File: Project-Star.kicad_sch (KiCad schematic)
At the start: 148 parts, among them J1 J_TH1, J2 J_TH2, Q1 DMN2004K, Q10 CSD18540Q5B, Q11 ZXMP10A13F, Q12 BSS123, Q13 ZXMP10A13F, Q2 DMN2004K, Q3 DMN2004K, Q4 DMN2004K, Q5 CSD19531Q5A, Q6 DMN2004K, Q7 DMN2004K, Q8 DMN2004K, Q9 DMN2004K, SW1 SW_SPST, U1 BQ7693006DBTR, U2 BQ76200PW, U3 LM5164DDA

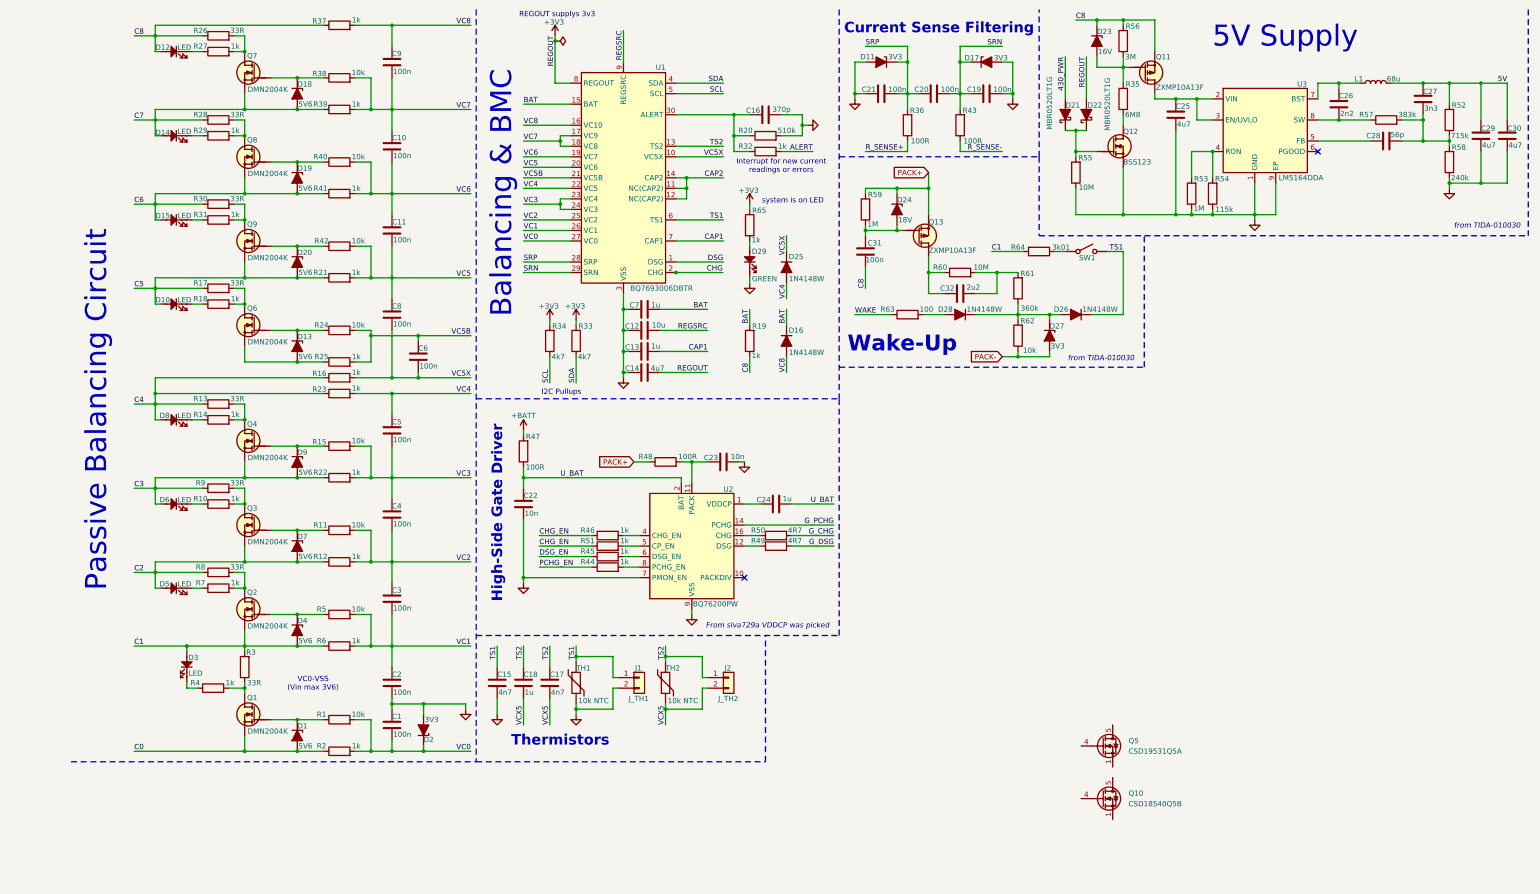
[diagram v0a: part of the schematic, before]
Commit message: cgr, dsg fets + jtag
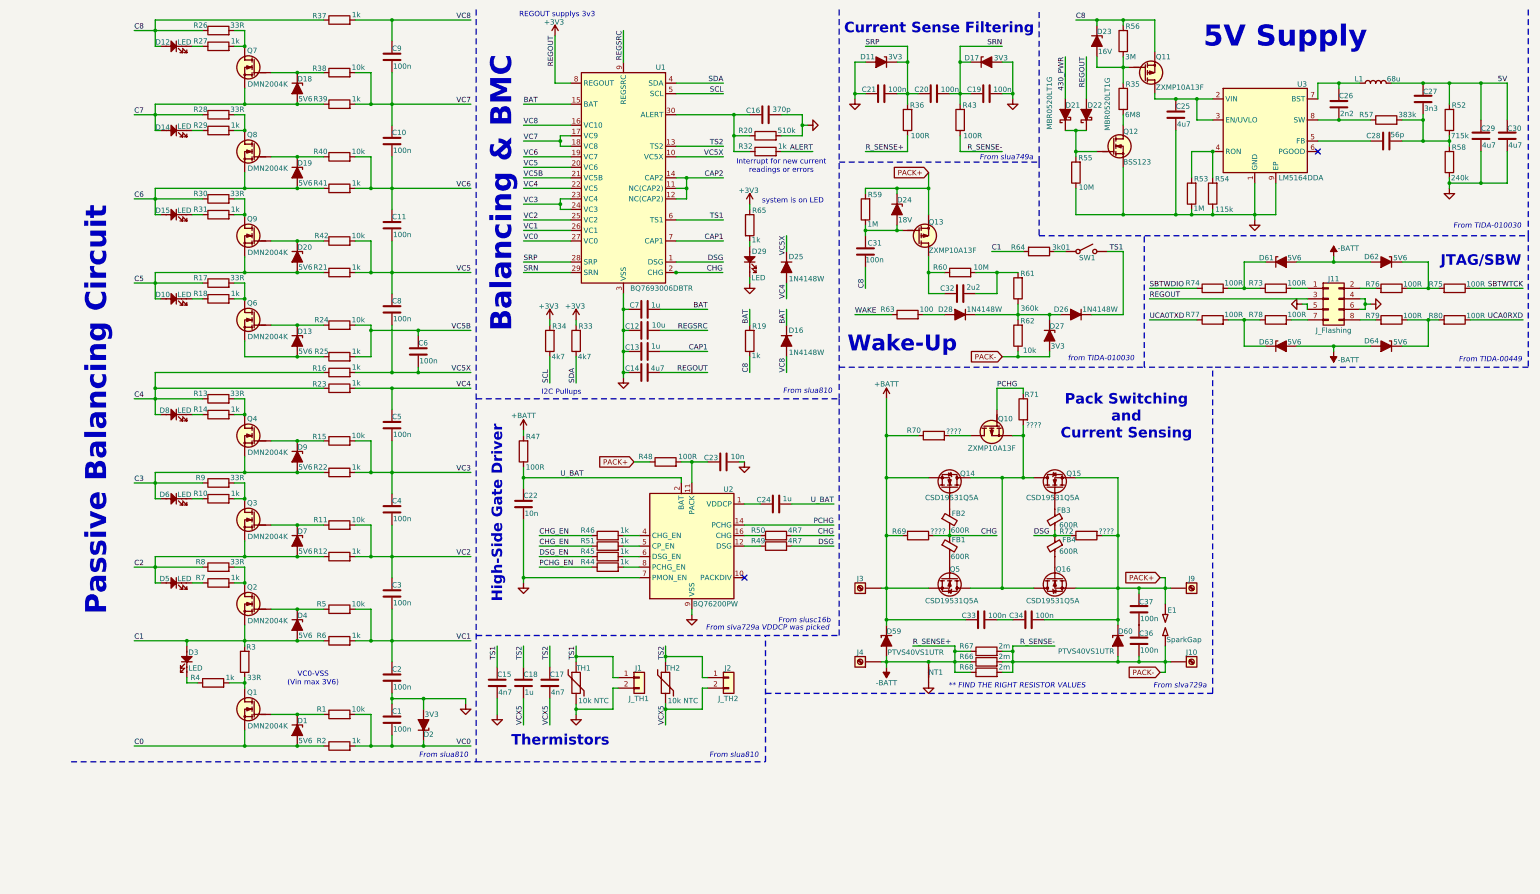
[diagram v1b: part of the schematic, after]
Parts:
- removed Q10: CSD18540Q5B, Package_TO_SOT_SMD:TDSON-8-1, symbol Transistor_FET:CSD18540Q5B
- added C33, C34, C36, C37: 100n, symbol Device:C
- added D59, D60: PTVS40VS1UTR, PCM_Diode_SMD_AKL:D_SOD-123F, symbol PCM_Diode_TVS_AKL:PTVS40VS1UTR
- added D61, D62, D63, D64: 5V6, symbol Device:D_Zener_Filled
- added E1: SparkGap, symbol Device:SparkGap
- added FB1, FB2, FB3, FB4: 600R, symbol Device:FerriteBead_Small
- added J10, J3, J4, J9: Screw_Terminal_01x01, symbol Connector:Screw_Terminal_01x01
- added J11: J_Flashing, 4ms_Connector:Pins_2x04_2.54mm_TH, symbol PCM_4ms_Connector:Conn_02x04
- added NT1: NetTie_2, symbol Device:NetTie_2
- added Q10: ZXMP10A13F, PCM_Package_TO_SOT_SMD_AKL:SOT-23, symbol PCM_Transistor_MOSFET_AKL:ZXMP10A13F
- added Q14, Q15, Q16: CSD19531Q5A, Package_TO_SOT_SMD:TDSON-8-1, symbol Transistor_FET:CSD19531Q5A
- added R66, R67, R68: 2m, symbol Device:R
- added R69, R70, R71, R72: ????, symbol Device:R
- added R73, R74, R75, R76, R77, R78, R79, R80: 100R, symbol Device:R
- D10, D12, D14, D15, D3, D5, D6, D8: footprint LED_THT:LED_D5.0mm -> PCM_Diode_SMD_AKL:D_0805_2012Metric
- D29: value GREEN -> LED; footprint LED_THT:LED_D5.0mm -> PCM_Diode_SMD_AKL:D_0805_2012Metric
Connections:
- net G_CHG is gone; now on net CHG: R50.2
- net G_DSG is gone; now on net DSG: R49.2
- net R_SENSE- is gone; now on net PACK-: R43.1
- net +3V3: now also J11.3 (Pin_3)
- net +BATT: now also Q5.1 (S), Q5.2 (S), Q5.3 (S), C33.1, D59.1 (K), J3.1 (Pin_1), Q14.1 (S), Q14.2 (S), Q14.3 (S), R69.2, R70.1
- net CHG: now also FB1.1, FB2.2, R69.1
- net DSG: now also FB3.2, FB4.1, R72.1
- net GND: now also J11.4 (Pin_4), J11.5 (Pin_5), J11.6 (Pin_6), NT1.1
- net PACK+: now also C34.2, C37.2, D60.1 (K), E1.2, J9.1 (Pin_1), Q15.1 (S), Q15.2 (S), Q15.3 (S), Q16.1 (S), Q16.2 (S), Q16.3 (S), R72.2
- net PACK-: now also C36.1, D60.2 (A), E1.1, J10.1 (Pin_1), R66.2, R67.2, R68.2
- net at Q5.4 (G): now also FB1.2
- net at Q5.5 (D): now also Q10.2 (S), Q14.5 (D), Q15.5 (D), Q16.5 (D), R71.2
- net G_PCHG renamed PCHG
- net PCHG: now also Q10.1 (G), R71.1
- net R_SENSE+ renamed -BATT
- net -BATT: now also D59.2 (A), D61.2 (A), D62.2 (A), D63.2 (A), D64.2 (A), J4.1 (Pin_1), NT1.2, R66.1, R67.1, R68.1
- new net: FB4.2, Q16.4 (G)
- new net: D61.1 (K), R73.1, R74.2
- new net: D63.1 (K), R77.2, R78.1
- new net: J11.7 (Pin_7), R78.2
- new net: D64.1 (K), R79.1, R80.2
- new net: J11.1 (Pin_1), R73.2
- new net: J11.2 (Pin_2), R76.2
- new net: J11.8 (Pin_8), R79.2
- new net: FB2.1, Q14.4 (G)
- new net: Q10.3 (D), R70.2
- new net: C36.2, C37.1
- new net: C33.2, C34.1
- new net: D62.1 (K), R75.2, R76.1
- new net: FB3.1, Q15.4 (G)
- new net SBTWDIO: R74.1
- new net SBTWTCK: R75.1
- new net UCA0RXD: R80.1
- new net UCA0TXD: R77.1
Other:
- note added: "** FIND THE RIGHT RESISTOR VALUES"
- note added: "From TIDA-00449"
- note added: "From TIDA-010030"
- note added: "From slua749a"
- note added: "From slua810"
- note added: "From slusc16b"
- note added: "From slva729a"
- note added: "JTAG/SBW"
- note added: "Pack Switching and Current Sensing"
- moved on the sheet: C1, C10, C11, C2, C3, C4, C5, C6, C8, C9, D1, D10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

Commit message: need to fix regsrc
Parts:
- removed SW1: SW_SPST, symbol Switch:SW_SPST
- added C73: 4u7, symbol Device:C
- added C74, C76: 100n, symbol Device:C
- added C75: 2n2, symbol Device:C
- added D30: 3V3, symbol Device:D_Zener_Filled
- added D31, D32, D33, D34, D65, D66, D67, D68: LED, PCM_Diode_SMD_AKL:D_0805_2012Metric, symbol PCM_SL_Devices:LED
- added Q17: CSD23381F4, symbol Device:Q_PMOS
- added Q18: TP0610K-T1-GE3, PCM_Package_TO_SOT_SMD_AKL:SOT-23, symbol PCM_Transistor_MOSFET_AKL:TP0610K
- added Q19: BSS138, PCM_Package_TO_SOT_SMD_AKL:SOT-23, symbol PCM_Transistor_MOSFET_AKL:BSS138
- added R81: 4k7, symbol Device:R
- added R82, R83, R87: 10k, symbol Device:R
- added R84: 154k, symbol Device:R
- added R85, R86: 1k, symbol Device:R
- added R88, R89, R90, R91, R92: 100k, symbol Device:R
- added SW1, SW3: Push_Button, Button_Switch_THT:SW_PUSH_6mm, symbol PCM_SL_Devices:Push_Button
- added U11: TPS3839G33DBZR, Package_TO_SOT_SMD:SOT-23, symbol Power_Supervisor:TPS3839DBZ
- added U5: LMT01LPG, Package_TO_SOT_THT:TO-92-2, symbol Sensor_Temperature:LMT01LPG
- added U6: MSP430G2553IPW28, Package_SO:TSSOP-28_4.4x9.7mm_P0.65mm, symbol MCU_Texas_MSP430:MSP430G2553IPW28
- R69, R71, R72: value ???? -> 100k
- R70: value ???? -> 1M
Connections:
- net +3V3: now also C73.2, C74.1, C76.1, Q17.D, R82.2, U11.3 (VDD), U6.1 (DVCC)
- net 430_PWR: now also U6.14 (P3.3/TA1.2)
- net ALERT: now also U6.2 (TA0CLK/ACLK/A0/CA0/P1.0)
- net C8: now also Q18.3 (D), R88.1
- net DSG_EN: now also U6.9 (P3.0/TA0.2)
- net GND: now also C73.1, C74.2, C75.2, C76.2, D30.2 (A), D31.1, D32.1, D33.1, D34.1, D65.1, D66.1, D67.1, D68.1, Q19.2 (S), R83.1, R87.1, R91.2, R92.2, SW1.1, U11.1 (GND), U6.28 (DVSS)
- net PACK-: now also R85.1
- net PCHG_EN: now also U6.8 (P3.1/TA1.0)
- net SBTWDIO: now also C75.1, R82.1, U6.24 (~{RST}/NMI/SBWTDIO)
- net SBTWTCK: now also U6.25 (SBWTCK/TEST)
- net SCL: now also U6.22 (TDI/TCLK/TA0.1/UCB0SOMI/UCB0SCL/A6/CA6/P1.6)
- net SDA: now also U6.23 (TDO/TDI/CAOUT/UCB0SIMO/UCB0SDA/A7/CA7/P1.7)
- net TS1: now also SW3.2
- net UCA0RXD: now also U6.3 (TA0.0/UCA0RXD/UCA0SOMI/A1/CA1/P1.1)
- net UCA0TXD: now also U6.4 (TA0.1/UCA0TXD/UCA0SIMO/A2/CA2/P1.2)
- net WAKE: now also U6.13 (P3.2/TA1.1)
- net at R64.1: now also SW3.1
- new net: Q17.S, R84.2
- new net: Q18.1 (G), R88.2, R89.1
- new net: R81.1, SW1.2
- new net: R81.2, U6.18 (TA1.2/P2.5)
- new net: R84.1, R85.2, R86.1, R87.2
- new net: Q18.2 (S), R90.1
- new net: Q19.3 (D), R89.2
- new net ISENSE: R86.2, U6.5 (ADC10CLK/CAOUT/VREF-/VeREF-/A3/CA3/P1.3)
- new net LED1: D65.2, U6.11 (TA1.1/P2.1)
- new net LED2: D66.2, U6.12 (TA1.1/P2.2)
- new net LED3: D67.2, U6.16 (TA1.0/P2.3)
- new net LED4: D68.2, U6.17 (TA1.2/P2.4)
- new net LED5: D31.2, U6.15 (P3.4/TA0.0)
- new net LED6: D32.2, U6.19 (P3.5/TA0.1)
- new net LED7: D33.2, U6.20 (P3.6/TA0.2)
- new net LED8: D34.2, U6.21 (P3.7/TA1CLK/CAOUT)
- new net PACK_READ_TMP: Q19.1 (G), R92.1, U5.2 (VP), U6.10 (TA1.0/P2.0)
- new net PACK_V: D30.1 (K), R90.2, R91.1, U6.6 (TCK/SMCLK/UCB0STE/UCA0CLK/VREF+/VeREF+/A4/CA4/P1.4)
- new net READ_ISENSE: Q17.G, U6.27 (TA0.1/XIN/P2.6)
- new net RST: U11.2 (~{RESET}), U6.26 (XOUT/P2.7)
- new net TMP: R83.2, U5.1 (VN), U6.7 (TMS/TA0.0/UCB0CLK/UCA0STE/A5/CA5/P1.5)
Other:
- removed sheet bk
- note added: "** MUST FIX REGSRC PIN based on datasheet **"
- note added: "Battery Level LEDs"
- note added: "Battery Management System Controller"
- note added: "From TIDA-00449 / TIDA-010030"
- note added: "MCU Current Sense"
- note added: "Read Voltage"
- note added: "Temperature Sensor"
- note added: "Verify the RST switch is placed right"
- note added: "Voltage Supervisor"

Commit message: commit before redesign of usb-c
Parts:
- removed C25, C29, C30: 4u7, symbol Device:C
- removed C26: 2n2, symbol Device:C
- removed C27: 3n3, symbol Device:C
- removed C28: 56p, symbol Device:C
- removed D21, D22: MBR0520LT1G, symbol PCM_Diode_Schottky_AKL:D_Schottky_Generic
- removed D23: 16V, symbol Device:D_Zener_Filled
- removed D32, D33, D34: LED, PCM_Diode_SMD_AKL:D_0805_2012Metric, symbol PCM_SL_Devices:LED
- removed J10, J9: Screw_Terminal_01x01, symbol Connector:Screw_Terminal_01x01
- removed L1: 68u, symbol Device:L
- removed Q11: ZXMP10A13F, PCM_Package_TO_SOT_SMD_AKL:SOT-23, symbol PCM_Transistor_MOSFET_AKL:ZXMP10A13F
- removed Q12: BSS123, PCM_Package_TO_SOT_SMD_AKL:SOT-23, symbol PCM_Transistor_MOSFET_AKL:BSS123
- removed R35: 6M8, symbol Device:R
- removed R52: 715k, symbol Device:R
- removed R53: 1M, symbol Device:R
- removed R54: 115k, symbol Device:R
- removed R55: 10M, symbol Device:R
- removed R56: 3M, symbol Device:R
- removed R57: 383k, symbol Device:R
- removed R58: 240k, symbol Device:R
- removed R81: 4k7, symbol Device:R
- removed U3: LM5164DDA, Package_SO:HSOP-8-1EP_3.9x4.9mm_P1.27mm_EP2.41x3.1mm_ThermalVias, symbol Regulator_Switching:LM5164DDA
- added C38, C39: 1u, symbol Device:C
- added C40, C41: 10u, symbol Device:C
- added D35: 1N4148W, PCM_Diode_SMD_AKL:D_SOD-123, symbol PCM_Diode_AKL:1N4148W
- added D69, D70, D71: LED, PCM_Diode_SMD_AKL:D_0805_2012Metric, symbol PCM_SL_Devices:LED
- added J5: Sense Terminals, 4ms_Connector:Pins_1x09_2.54mm_TH, symbol PCM_4ms_Connector:Conn_01x09
- added J6: BMS_I2C, symbol Connector_Generic:Conn_01x05
- added J7, J8: Screw_Terminal_01x01, symbol Connector:Screw_Terminal_01x01
- added Q20: BSS123, PCM_Package_TO_SOT_SMD_AKL:SOT-23, symbol PCM_Transistor_MOSFET_AKL:BSS123
- added R100, R97, R99: 100R, symbol Device:R
- added R93, R98: 1k, symbol Device:R
- added R94: 2m, symbol Device:R
- added R95: 0R, symbol Device:R
- added R96: 100k, symbol Device:R
- added SW3, SW4: SW_DPST, symbol Switch:SW_DPST
- C75: value 2n2 -> 2.2n
- R82: value 10k -> 47k
- renumbered SW3 to SW1, SW1 to SW2
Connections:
- net 430_PWR is gone; now on net LED6: U6.14 (P3.3/TA1.2)
- net +BATT: no longer J3.1 (Pin_1), Q5.1 (S), Q5.2 (S), Q5.3 (S)
- net -BATT: now also R94.1, SW3.2; no longer J4.1 (Pin_1)
- net ALERT: now also J6.4 (Pin_4)
- net BAT: now also C40.2, R93.1
- net C0: now also J5.1 (Pin_1)
- net C1: now also J5.2 (Pin_2)
- net C2: now also J5.3 (Pin_3)
- net C3: now also J5.4 (Pin_4)
- net C4: now also J5.5 (Pin_5)
- net C5: now also J5.6 (Pin_6)
- net C6: now also J5.7 (Pin_7)
- net C7: now also J5.8 (Pin_8)
- net C8: now also D35.2 (A), J5.9 (Pin_9), R93.2, R96.1
- net GND: now also C38.1, C39.1, C41.1, D69.1, D70.1, D71.1, J6.5 (Pin_5); no longer C74.2
- net LED5: now also U6.18 (TA1.2/P2.5); no longer U6.15 (P3.4/TA0.0)
- net LED6: now also D69.2; no longer U6.19 (P3.5/TA0.1)
- net LED7: now also U6.15 (P3.4/TA0.0), D70.2; no longer U6.20 (P3.6/TA0.2)
- net LED8: now also U6.19 (P3.5/TA0.1), D71.2; no longer U6.21 (P3.7/TA1CLK/CAOUT)
- net PACK+: now also SW4.3
- net PACK-: now also R94.2, SW4.1
- net REGSRC: now also C38.2, Q20.2 (S)
- net SBTWDIO: now also SW2.2
- net SCL: now also R99.1
- net SDA: now also R100.1
- net VC5X: now also C40.1, C41.2, R98.1
- net PACK: now reaches C23.1, R48.2, U2.11 (PACK)
- net +3V3 renamed REGOUT
- net REGOUT: now also R95.1
- new net: J8.1 (Pin_1), SW4.2
- new net: J7.1 (Pin_1), SW4.4
- new net: J6.2 (Pin_2), R99.2
- new net: J4.1 (Pin_1), SW3.1
- new net: D35.1 (K), R96.2, R97.1
- new net: Q20.1 (G), R98.2
- new net: J6.1 (Pin_1), R95.2
- new net: J6.3 (Pin_3), R100.2
- new net: J3.1 (Pin_1), SW3.3
- new net: C39.2, Q20.3 (D), R97.2
- new net PD_I2Ct_SCL: U6.21 (P3.7/TA1CLK/CAOUT)
- new net PD_I2Ct_SDA: U6.20 (P3.6/TA0.2)
- new net SCREW_BATT+: Q5.1 (S), Q5.2 (S), Q5.3 (S), SW3.4
- no-connect marks 2 -> 1
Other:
- added sheet USB-C-PD3.0 (USB-C-PD3.0.kicad_sch)
- note added: "BMS Protection Board for 8S Battery Pack In/Out: min voltage: 24.0 V, nominal voltage: 29.6 V, max voltage: 33.6 V Output: 30A continuous discharge current, 100A peak discharge current"
- note added: "CONN Headers"
- note added: "High Voltage REGSRC Supply"
- note added: "PD I2C Lines have pullup's already"
- note added: "PWR FLAGs"
- note added: "Screw Terminals"
- note added: "TODO: Add USB-C to Flash board"
- note added: "Understand how this works"
- note added: "from slua810"
- note removed: "** FIND THE RIGHT RESISTOR VALUES"
- note removed: "** MUST FIX REGSRC PIN based on datasheet **"
- note removed: "5V Supply"
- note removed: "From TIDA-010030"
- note removed: "Verify the RST switch is placed right"
- moved on the sheet: C23, D31, D65, D66, D67, D68, Q17, R48, R84, R85, R86, R87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
